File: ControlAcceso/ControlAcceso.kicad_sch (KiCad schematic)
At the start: 7 parts, among them J1 Conn_01x03, J2 Conn_01x07

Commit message: Cambios
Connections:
- net LED-OFF: now also A1.6 (D3); no longer A1.12 (D9)
- net LED-OK: now also A1.5 (D2); no longer A1.11 (D8)
- net OUT: now also A1.7 (D4)
- net CS renamed SPI
- new net RST: A1.12 (D9)
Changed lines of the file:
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@@
   (junction (at 146.05 97.79) (diameter 0) (color 0 0 0 0)
   )
-  (wire (pts (xy 132.08 77.47) (xy 120.65 77.47))
-    (stroke (width 0) (type default))
-  )
   (wire (pts (xy 186.69 49.53) (xy 187.96 49.53))
     (stroke (width 0) (type default))
   )
+  (wire (pts (xy 119.38 64.77) (xy 132.08 64.77))
+    (stroke (width 0) (type default))
+  )
   (wire (pts (xy 71.12 81.28) (xy 78.74 81.28))
     (stroke (width 0) (type default))
@@
     (stroke (width 0) (type default))
   )
+  (wire (pts (xy 118.11 80.01) (xy 132.08 80.01))
+    (stroke (width 0) (type default))
+  )
   (wire (pts (xy 62.23 81.28) (xy 71.12 81.28))
     (stroke (width 0) (type default))
@@
     (stroke (width 0) (type default))
   )
-  (wire (pts (xy 118.11 77.47) (xy 115.57 77.47))
+  (wire (pts (xy 119.38 67.31) (xy 132.08 67.31))
     (stroke (width 0) (type default))
   )
@@
     (stroke (width 0) (type default))
   )
-  (wire (pts (xy 132.08 80.01) (xy 118.11 80.01))
-    (stroke (width 0) (type default))
-  )
-  (wire (pts (xy 118.11 80.01) (xy 118.11 77.47))
-    (stroke (width 0) (type default))
-  )
   (wire (pts (xy 62.23 63.5) (xy 62.23 67.31))
     (stroke (width 0) (type default))
@@
     (stroke (width 0) (type default))
   )
-  (wire (pts (xy 120.65 77.47) (xy 120.65 73.66))
-    (stroke (width 0) (type default))
-  )
   (wire (pts (xy 193.04 53.34) (xy 186.69 53.34))
     (stroke (width 0) (type default))
@@
     (stroke (width 0) (type default))
   )
-  (wire (pts (xy 120.65 73.66) (xy 114.3 73.66))
+  (wire (pts (xy 119.38 62.23) (xy 132.08 62.23))
     (stroke (width 0) (type default))
   )
@@
     (effects (font (size 2 2) (thickness 0.254) bold) (justify left bottom))
   )
-  (global_label "CS" (shape input) (at 118.11 82.55 180) (fields_autoplaced)
+  (global_label "SPI" (shape input) (at 118.11 82.55 180) (fields_autoplaced)
     (effects (font (size 1.27 1.27)) (justify right))
-    (property "Intersheetrefs" "${INTERSHEET_REFS}" (at 112.7247 82.55 0)
+    (property "Intersheetrefs" "${INTERSHEET_REFS}" (at 112.1199 82.55 0)
       (effects (font (size 1.27 1.27)) (justify right) hide)
     )
@@
     )
   )
+  (global_label "OUT" (shape input) (at 119.38 67.31 180) (fields_autoplaced)
+    (effects (font (size 1.27 1.27) bold) (justify right))
+    (property "Intersheetrefs" "${INTERSHEET_REFS}" (at 112.4172 67.31 0)
+      (effects (font (size 1.27 1.27)) (justify right) hide)
+    )
+  )
   (global_label "LED-OFF" (shape input) (at 76.2 46.99 180) (fields_autoplaced)
     (effects (font (size 1.27 1.27) bold) (justify right))
@@
     )
   )
-  (global_label "LED-OK" (shape input) (at 114.3 73.66 180) (fields_autoplaced)
-    (effects (font (size 1.27 1.27) bold) (justify right))
-    (property "Intersheetrefs" "${INTERSHEET_REFS}" (at 103.3458 73.66 0)
+  (global_label "LED-OK" (shape input) (at 119.38 62.23 180) (fields_autoplaced)
+    (effects (font (size 1.27 1.27) bold) (justify right))
+    (property "Intersheetrefs" "${INTERSHEET_REFS}" (at 108.4258 62.23 0)
       (effects (font (size 1.27 1.27)) (justify right) hide)
     )
@@
     )
   )
-  (global_label "LED-OFF" (shape input) (at 115.57 77.47 180) (fields_autoplaced)
-    (effects (font (size 1.27 1.27) bold) (justify right))
-    (property "Intersheetrefs" "${INTERSHEET_REFS}" (at 103.7086 77.47 0)
+  (global_label "LED-OFF" (shape input) (at 119.38 64.77 180) (fields_autoplaced)
+    (effects (font (size 1.27 1.27) bold) (justify right))
+    (property "Intersheetrefs" "${INTERSHEET_REFS}" (at 107.5186 64.77 0)
       (effects (font (size 1.27 1.27)) (justify right) hide)
     )
@@
     )
   )
+  (global_label "RST" (shape input) (at 118.11 80.01 180) (fields_autoplaced)
+    (effects (font (size 1.27 1.27) bold) (justify right))
+    (property "Intersheetrefs" "${INTERSHEET_REFS}" (at 111.3287 80.01 0)
+      (effects (font (size 1.27 1.27)) (justify right) hide)
+    )
+  )

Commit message: Ultimo
Generación de archivos GERBER, modificacion de rutas
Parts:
- added R3: 0, Resistor_THT:R_Axial_DIN0207_L6.3mm_D2.5mm_P10.16mm_Horizontal, symbol PCM_SL_Resistors:220ohm
- A1: value Arduino_Nano_v2.x -> Arduino_Nano_33_IoT
- D2: footprint (none) -> LED_THT:LED_D5.0mm
- renumbered J2 to RFID1, J1 to Salida1
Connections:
- net +5V: no longer RFID1.1 (Pin_1)
- net 3V3: now also RFID1.1 (Pin_1)
- net MISO: now also RFID1.5 (Pin_5)
- net MOSI: now also RFID1.4 (Pin_4)
- net OUT: now also R3.2; no longer Salida1.2 (Pin_2)
- net RST: now also RFID1.2 (Pin_2)
- net SCK: now also RFID1.6 (Pin_6)
- net SPI: now also RFID1.3 (Pin_3)
- net LED-OK renamed LED-ON
- new net: R3.1, Salida1.2 (Pin_2)
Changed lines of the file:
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@@
   (junction (at 146.05 97.79) (diameter 0) (color 0 0 0 0)
   )
-  (wire (pts (xy 186.69 49.53) (xy 187.96 49.53))
-    (stroke (width 0) (type default))
-  )
   (wire (pts (xy 119.38 64.77) (xy 132.08 64.77))
     (stroke (width 0) (type default))
@@
     (stroke (width 0) (type default))
   )
-  (wire (pts (xy 189.23 73.66) (xy 196.85 73.66))
+  (wire (pts (xy 187.96 73.66) (xy 196.85 73.66))
     (stroke (width 0) (type default))
   )
@@
     (stroke (width 0) (type default))
   )
+  (wire (pts (xy 193.04 53.34) (xy 187.96 53.34))
+    (stroke (width 0) (type default))
+  )
   (wire (pts (xy 119.38 67.31) (xy 132.08 67.31))
     (stroke (width 0) (type default))
@@
     (stroke (width 0) (type default))
   )
+  (wire (pts (xy 196.85 76.2) (xy 180.34 76.2))
+    (stroke (width 0) (type default))
+  )
   (wire (pts (xy 147.32 46.99) (xy 147.32 39.37))
     (stroke (width 0) (type default))
@@
     (stroke (width 0) (type default))
   )
-  (wire (pts (xy 187.96 49.53) (xy 187.96 50.8))
+  (wire (pts (xy 187.96 44.45) (xy 187.96 50.8))
     (stroke (width 0) (type default))
   )
@@
     (stroke (width 0) (type default))
   )
+  (wire (pts (xy 180.34 53.34) (xy 172.72 53.34))
+    (stroke (width 0) (type default))
+  )
   (wire (pts (xy 147.32 39.37) (xy 151.13 39.37))
     (stroke (width 0) (type default))
   )
+  (wire (pts (xy 196.85 86.36) (xy 180.34 86.36))
+    (stroke (width 0) (type default))
+  )
+  (wire (pts (xy 196.85 83.82) (xy 187.96 83.82))
+    (stroke (width 0) (type default))
+  )
   (wire (pts (xy 193.04 55.88) (xy 181.61 55.88))
     (stroke (width 0) (type default))
   )
+  (wire (pts (xy 196.85 78.74) (xy 187.96 78.74))
+    (stroke (width 0) (type default))
+  )
   (wire (pts (xy 144.78 97.79) (xy 146.05 97.79))
     (stroke (width 0) (type default))
   )
-  (wire (pts (xy 193.04 53.34) (xy 186.69 53.34))
+  (wire (pts (xy 196.85 81.28) (xy 180.34 81.28))
+    (stroke (width 0) (type default))
+  )
+  (wire (pts (xy 187.96 69.85) (xy 187.96 73.66))
     (stroke (width 0) (type default))
   )
@@
     )
   )
-  (global_label "OUT" (shape input) (at 186.69 53.34 180) (fields_autoplaced)
-    (effects (font (size 1.27 1.27) bold) (justify right))
-    (property "Intersheetrefs" "${INTERSHEET_REFS}" (at 179.7272 53.34 0)
+  (global_label "OUT" (shape input) (at 172.72 53.34 180) (fields_autoplaced)
+    (effects (font (size 1.27 1.27) bold) (justify right))
+    (property "Intersheetrefs" "${INTERSHEET_REFS}" (at 165.7572 53.34 0)
       (effects (font (size 1.27 1.27)) (justify right) hide)
     )
@@
     )
   )
-  (global_label "+5V" (shape input) (at 189.23 73.66 180) (fields_autoplaced)
-    (effects (font (size 1.27 1.27) bold) (justify right))
-    (property "Intersheetrefs" "${INTERSHEET_REFS}" (at 182.0253 73.66 0)
-      (effects (font (size 1.27 1.27)) (justify right) hide)
-    )
-  )
-  (global_label "LED-OK" (shape input) (at 119.38 62.23 180) (fields_autoplaced)
-    (effects (font (size 1.27 1.27) bold) (justify right))
-    (property "Intersheetrefs" "${INTERSHEET_REFS}" (at 108.4258 62.23 0)
-      (effects (font (size 1.27 1.27)) (justify right) hide)
-    )
-  )
-  (global_label "+5V" (shape input) (at 186.69 49.53 180) (fields_autoplaced)
-    (effects (font (size 1.27 1.27) bold) (justify right))
-    (property "Intersheetrefs" "${INTERSHEET_REFS}" (at 179.4853 49.53 0)
-      (effects (font (size 1.27 1.27)) (justify right) hide)
-    )
-  )
-  (global_label "LED-OK" (shape input) (at 60.96 46.99 180) (fields_autoplaced)
-    (effects (font (size 1.27 1.27) bold) (justify right))
-    (property "Intersheetrefs" "${INTERSHEET_REFS}" (at 50.0058 46.99 0)
+  (global_label "LED-ON" (shape input) (at 119.38 62.23 180) (fields_autoplaced)
+    (effects (font (size 1.27 1.27) bold) (justify right))
+    (property "Intersheetrefs" "${INTERSHEET_REFS}" (at 108.2383 62.23 0)
+      (effects (font (size 1.27 1.27)) (justify right) hide)
+    )
+  )
+  (global_label "SCK" (shape input) (at 180.34 86.36 180) (fields_autoplaced)
+    (effects (font (size 1.27 1.27)) (justify right))
+    (property "Intersheetrefs" "${INTERSHEET_REFS}" (at 173.6847 86.36 0)
+      (effects (font (size 1.27 1.27)) (justify right) hide)
+    )
+  )
+  (global_label "SPI" (shape input) (at 187.96 78.74 180) (fields_autoplaced)
+    (effects (font (size 1.27 1.27)) (justify right))
+    (property "Intersheetrefs" "${INTERSHEET_REFS}" (at 181.9699 78.74 0)
+      (effects (font (size 1.27 1.27)) (justify right) hide)
+    )
+  )
+  (global_label "MOSI" (shape input) (at 180.34 81.28 180) (fields_autoplaced)
+    (effects (font (size 1.27 1.27)) (justify right))
+    (property "Intersheetrefs" "${INTERSHEET_REFS}" (at 172.838 81.28 0)
+      (effects (font (size 1.27 1.27)) (justify right) hide)
+    )
+  )
+  (global_label "+5V" (shape input) (at 187.96 44.45 180) (fields_autoplaced)
+    (effects (font (size 1.27 1.27) bold) (justify right))
+    (property "Intersheetrefs" "${INTERSHEET_REFS}" (at 180.7553 44.45 0)
+      (effects (font (size 1.27 1.27)) (justify right) hide)
+    )
+  )
+  (global_label "MISO" (shape input) (at 187.96 83.82 180) (fields_autoplaced)
+    (effects (font (size 1.27 1.27)) (justify right))
+    (property "Intersheetrefs" "${INTERSHEET_REFS}" (at 180.458 83.82 0)
+      (effects (font (size 1.27 1.27)) (justify right) hide)
+    )
+  )
+  (global_label "LED-ON" (shape input) (at 60.96 46.99 180) (fields_autoplaced)
+    (effects (font (size 1.27 1.27) bold) (justify right))
+    (property "Intersheetrefs" "${INTERSHEET_REFS}" (at 49.8183 46.99 0)
       (effects (font (size 1.27 1.27)) (justify right) hide)
     )
@@
     )
   )
+  (global_label "RST" (shape input) (at 180.34 76.2 180) (fields_autoplaced)
+    (effects (font (size 1.27 1.27) bold) (justify right))
+    (property "Intersheetrefs" "${INTERSHEET_REFS}" (at 173.5587 76.2 0)
+      (effects (font (size 1.27 1.27)) (justify right) hide)
+    )
+  )
   (global_label "RST" (shape input) (at 118.11 80.01 180) (fields_autoplaced)
     (effects (font (size 1.27 1.27) bold) (justify right))
@@
     (effects (font (size 1.27 1.27)) (justify right))
     (property "Intersheetrefs" "${INTERSHEET_REFS}" (at 111.4547 90.17 0)
+      (effects (font (size 1.27 1.27)) (justify right) hide)
+    )
+  )
+  (global_label "3V3" (shape input) (at 187.96 69.85 180) (fields_autoplaced)
+    (effects (font (size 1.27 1.27) bold) (justify right))
+    (property "Intersheetrefs" "${INTERSHEET_REFS}" (at 181.1182 69.85 0)
       (effects (font (size 1.27 1.27)) (justify right) hide)
     )
@@
       (effects (font (size 1.27 1.27)) (justify right))
     )
-    (property "Footprint" "" (at 78.74 71.12 0)
+    (property "Footprint" "LED_THT:LED_D5.0mm" (at 78.74 71.12 0)
       (effects (font (size 1.27 1.27)) hide)
     )
@@
         (path "/01db9da7-ae97-4914-ace0-84de2f5ab849"
           (reference "D2") (unit 1)
+        )
+      )
+    )
+  )
+  (symbol (lib_id "PCM_SL_Resistors:220ohm") (at 184.15 53.34 180) (unit 1)
+    (in_bom yes) (on_board yes) (dnp no) (fields_autoplaced)
+    (property "Reference" "R3" (at 184.15 46.99 0)
+      (effects (font (size 1.27 1.27)))
+    )
+    (property "Value" "0" (at 184.15 49.53 0)
+      (effects (font (size 1.27 1.27)))
+    )
+    (property "Footprint" "Resistor_THT:R_Axial_DIN0207_L6.3mm_D2.5mm_P10.16mm_Horizontal" (at 183.261 49.022 0)
+      (effects (font (size 1.27 1.27)) hide)
+    )
+    (property "Datasheet" "" (at 183.642 53.34 0)
+      (effects (font (size 1.27 1.27)) hide)
+    )
+    (pin "1")
+    (pin "2")
+    (instances
+      (project "ControlAcceso"
+        (path "/01db9da7-ae97-4914-ace0-84de2f5ab849"
+          (reference "R3") (unit 1)
         )
       )
@@
       (effects (font (size 1.27 1.27)) (justify left))
     )
-    (property "Value" "Arduino_Nano_v2.x" (at 149.2759 100.33 0)
+    (property "Value" "Arduino_Nano_33_IoT" (at 149.2759 100.33 0)
       (effects (font (size 1.27 1.27)) (justify left))
     )
@@
   (symbol (lib_id "Connector_Generic:Conn_01x07") (at 201.93 81.28 0) (unit 1)
     (in_bom yes) (on_board yes) (dnp no) (fields_autoplaced)
-    (property "Reference" "J2" (at 204.47 80.01 0)
+    (property "Reference" "RFID1" (at 204.47 80.01 0)
       (effects (font (size 1.27 1.27)) (justify left))
     )
@@
       (project "ControlAcceso"
         (path "/01db9da7-ae97-4914-ace0-84de2f5ab849"
-          (reference "J2") (unit 1)
+          (reference "RFID1") (unit 1)
         )
       )
@@
   (symbol (lib_id "PCM_4ms_Connector:Conn_01x03") (at 198.12 53.34 0) (unit 1)
     (in_bom yes) (on_board yes) (dnp no) (fields_autoplaced)
-    (property "Reference" "J1" (at 200.66 52.07 0)
+    (property "Reference" "Salida1" (at 200.66 52.07 0)
       (effects (font (size 1.27 1.27)) (justify left))
     )
@@
       (project "ControlAcceso"
         (path "/01db9da7-ae97-4914-ace0-84de2f5ab849"
-          (reference "J1") (unit 1)
-        )
-      )
+          (reference "Salida1") (unit 1)
+        )
+      )

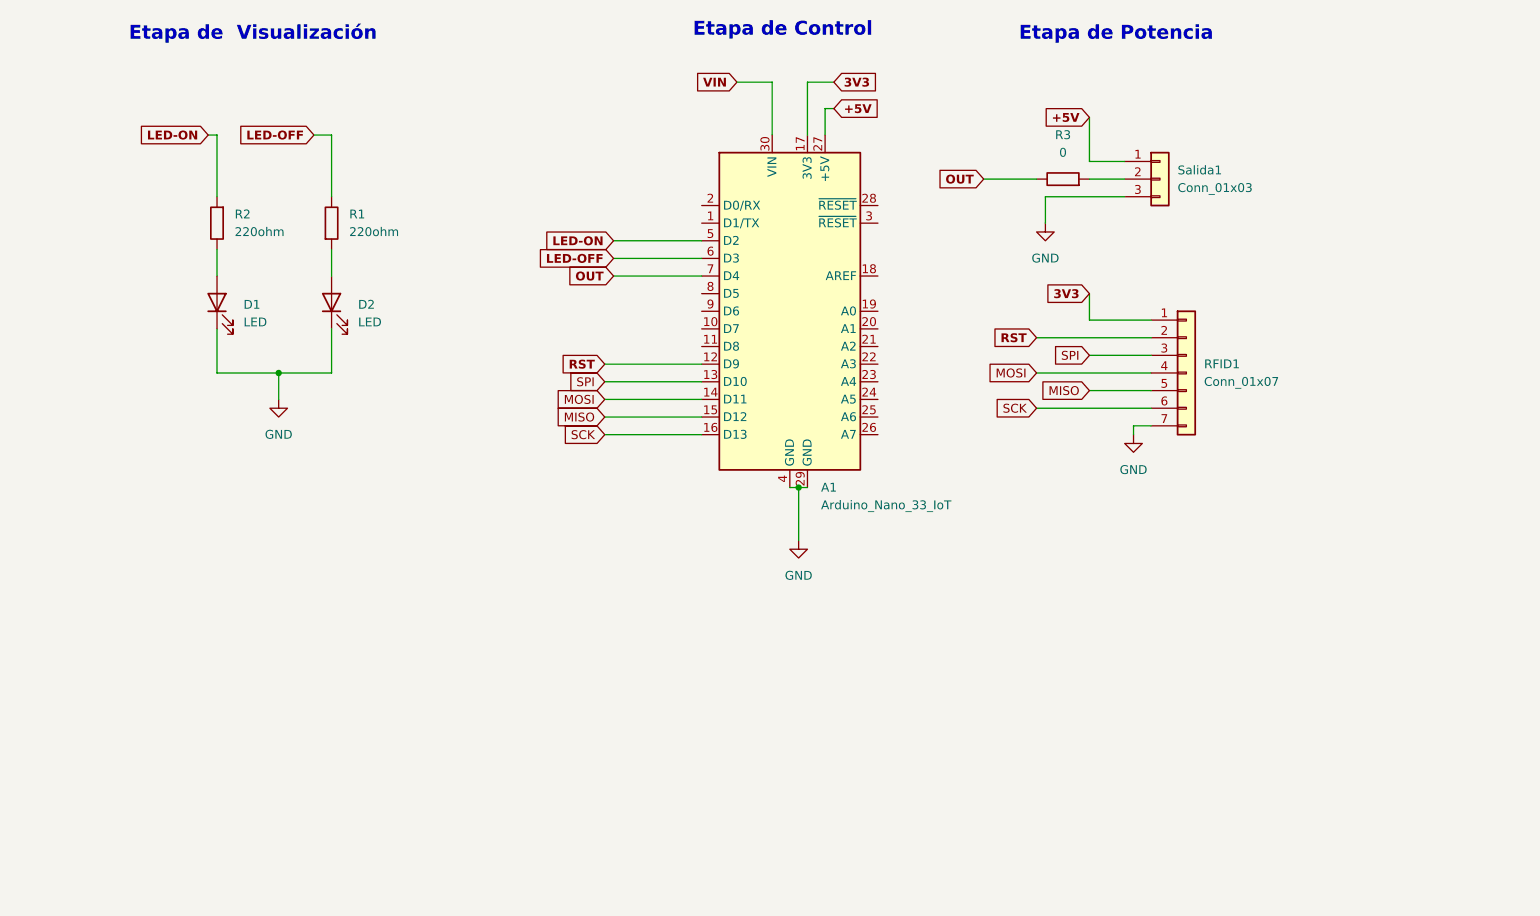
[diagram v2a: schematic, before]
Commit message: Cambios Significativos
Se quito codigo de prueba, se cambio modulo RFID y se agrego  regulador 7805.
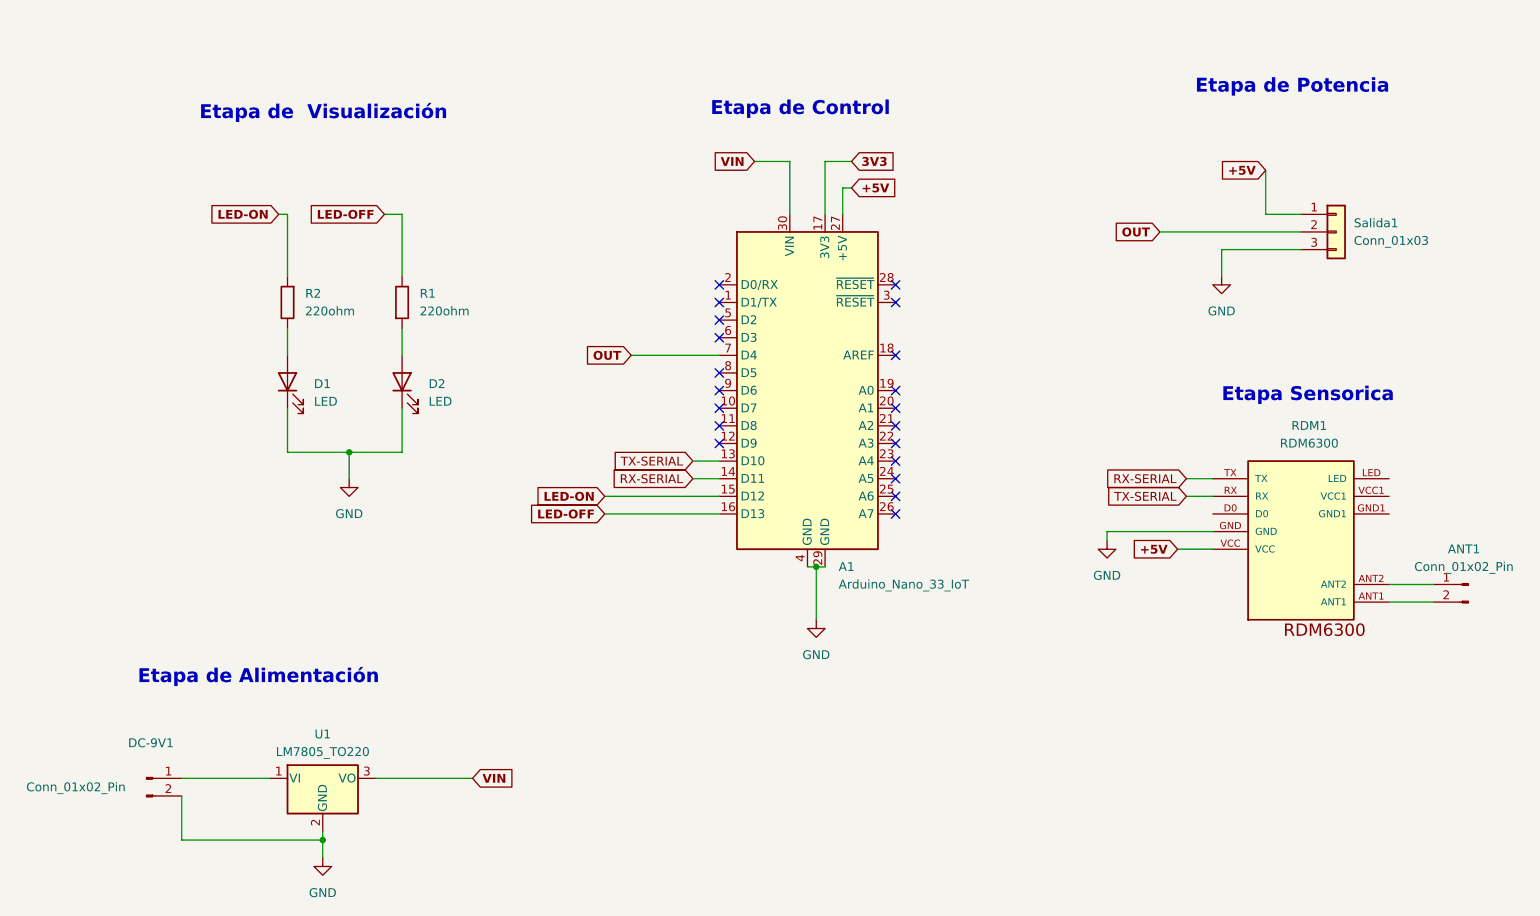
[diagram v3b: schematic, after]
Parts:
- removed R3: 0, Resistor_THT:R_Axial_DIN0207_L6.3mm_D2.5mm_P10.16mm_Horizontal, symbol PCM_SL_Resistors:220ohm
- removed RFID1: Conn_01x07, Connector_Molex:Molex_SL_171971-0007_1x07_P2.54mm_Vertical, symbol Connector_Generic:Conn_01x07
- added ANT1, DC-9V1: Conn_01x02_Pin, Connector_PinHeader_2.54mm:PinHeader_1x02_P2.54mm_Vertical, symbol Connector:Conn_01x02_Pin
- added RDM1: RDM6300, RDM6300:RDM6300, symbol RDM6300:RDM6300
- added U1: LM7805_TO220, Package_TO_SOT_THT:TO-220-3_Vertical, symbol Regulator_Linear:LM7805_TO220
- Salida1: footprint Connector:FanPinHeader_1x03_P2.54mm_Vertical -> Connector_PinHeader_2.54mm:PinHeader_1x03_P2.54mm_Vertical
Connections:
- net MISO is gone; now on net LED-ON: A1.15 (D12)
- net SCK is gone; now on net LED-OFF: A1.16 (D13)
- net +5V: now also RDM1.VCC
- net GND: now also DC-9V1.2 (Pin_2), RDM1.GND, U1.2 (GND)
- net LED-OFF: no longer A1.6 (D3)
- net LED-ON: no longer A1.5 (D2)
- net OUT: now also Salida1.2 (Pin_2)
- net VIN: now also U1.3 (VO)
- net MOSI renamed RX-SERIAL
- net RX-SERIAL: now also RDM1.TX
- net RST: no longer names the net of A1.12 (D9)
- net SPI renamed TX-SERIAL
- net TX-SERIAL: now also RDM1.RX
- new net: ANT1.2 (Pin_2), RDM1.ANT1
- new net: ANT1.1 (Pin_1), RDM1.ANT2
- new net: DC-9V1.1 (Pin_1), U1.1 (VI)
- no-connect marks 0 -> 20
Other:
- note added: "Etapa Sensorica"
- note added: "Etapa de Alimentación"
- moved on the sheet: A1, D1, D2, R1, R2, Salida1
